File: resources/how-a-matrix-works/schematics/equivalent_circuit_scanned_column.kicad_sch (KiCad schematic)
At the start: 10 parts

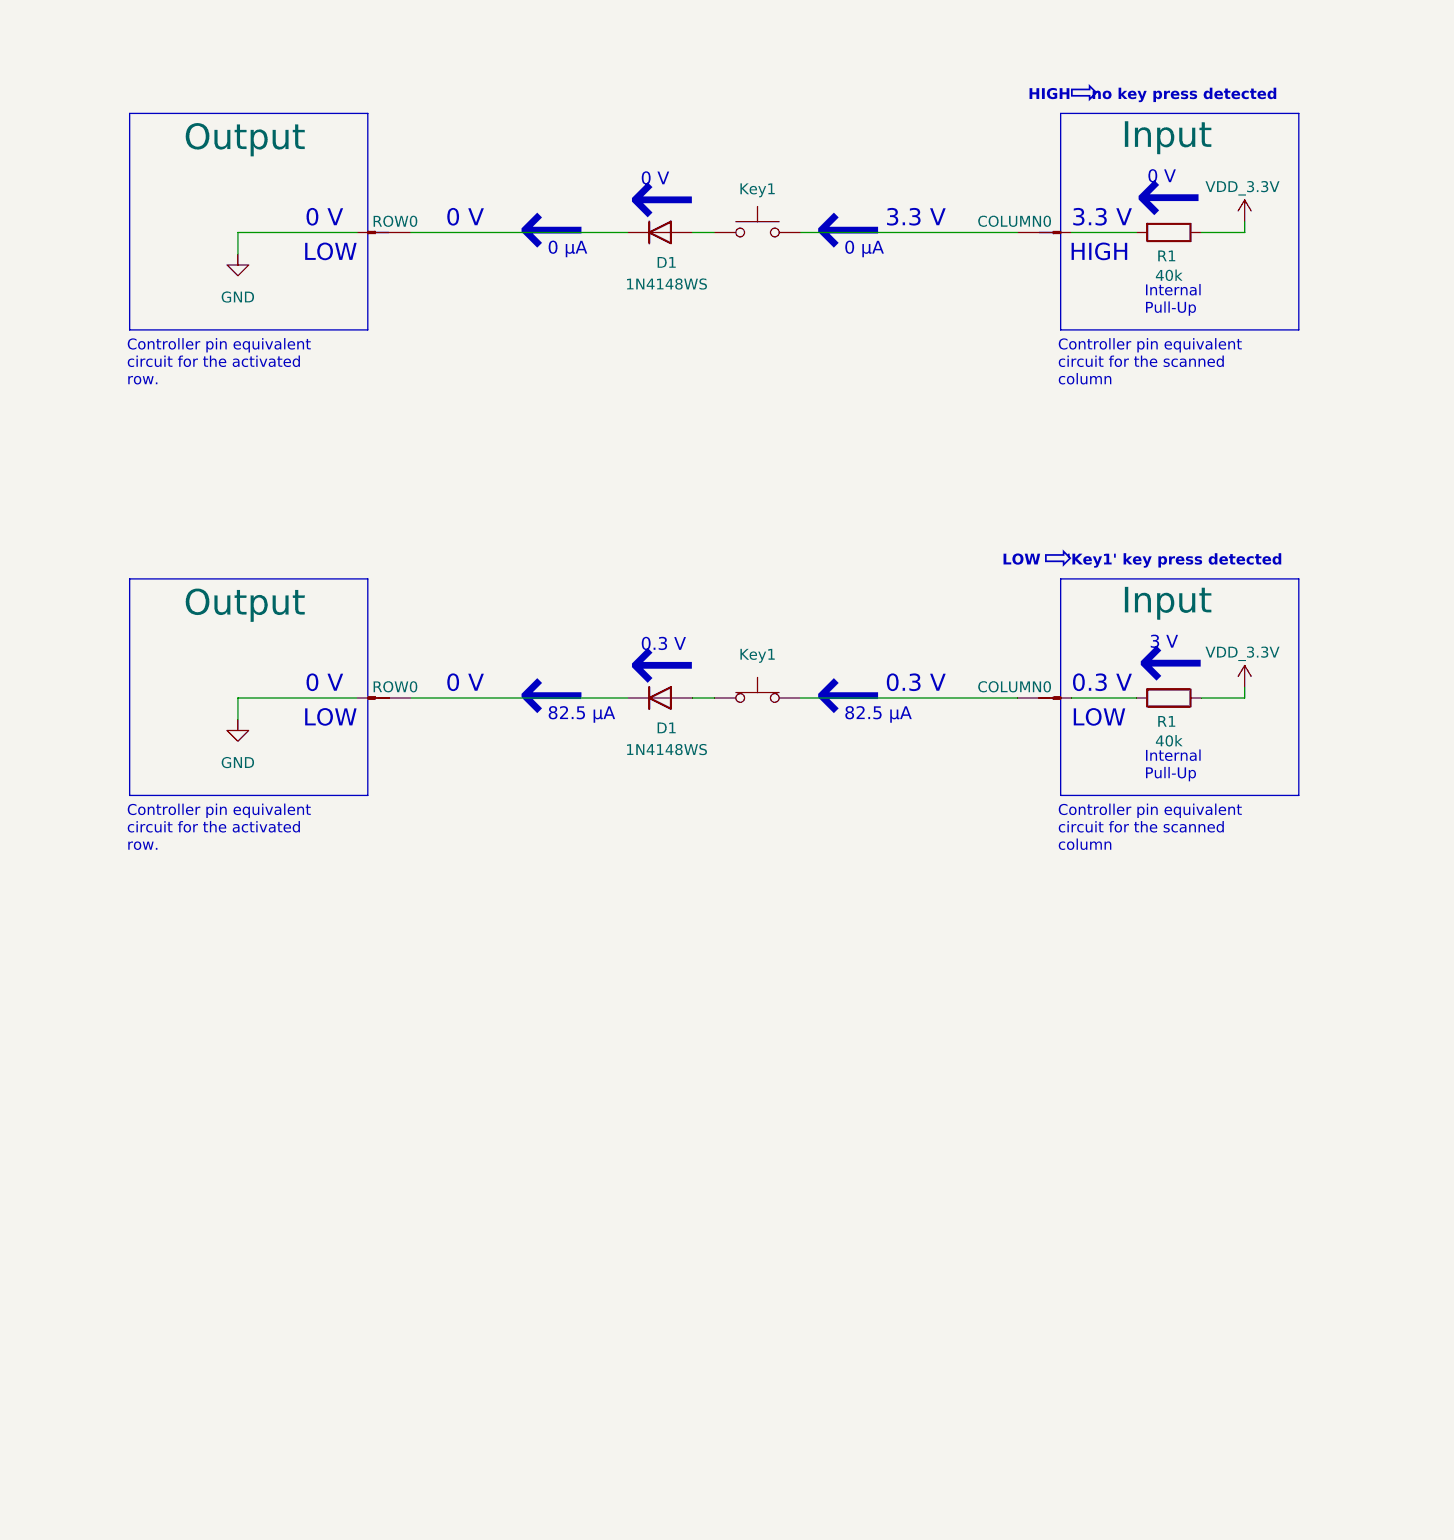
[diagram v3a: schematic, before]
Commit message: refactor equivalent circuit schematic and images
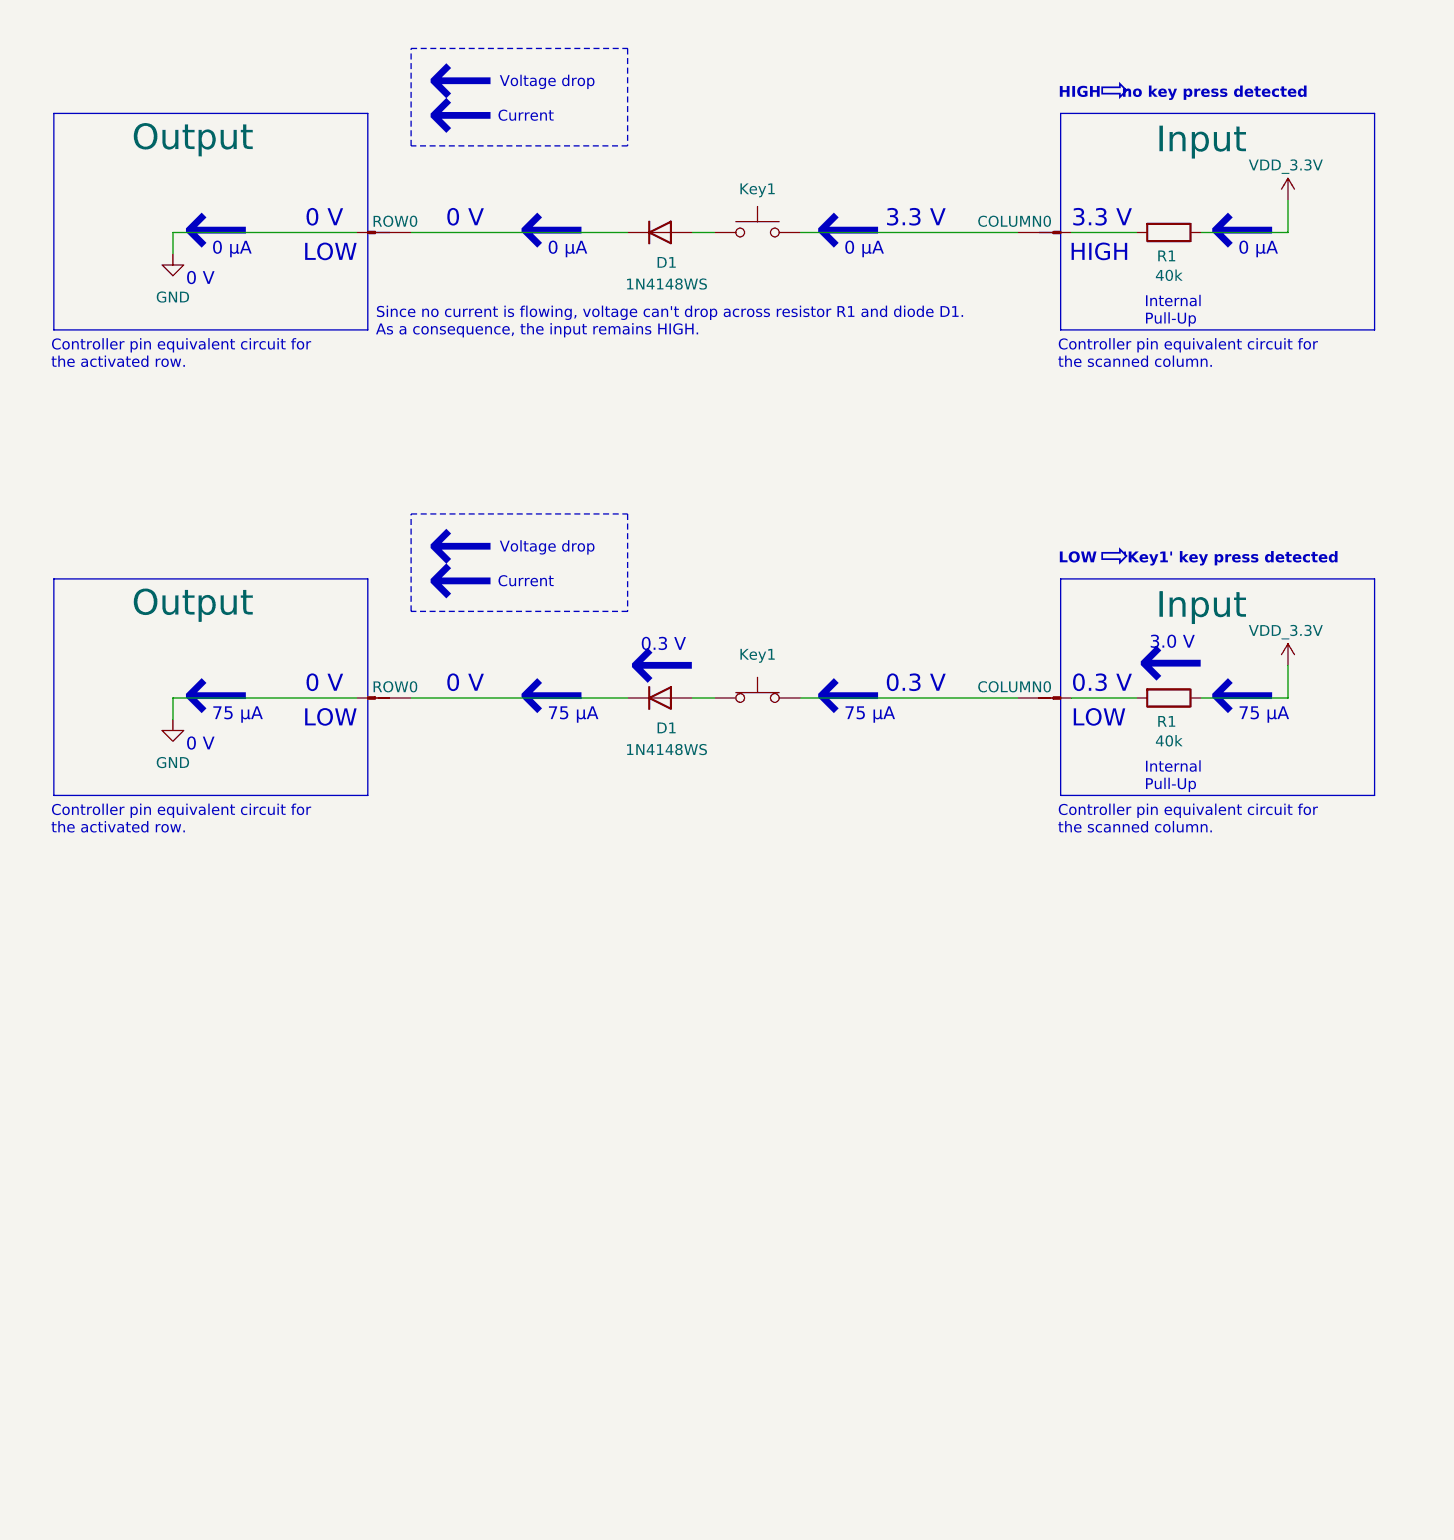
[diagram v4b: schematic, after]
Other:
- note added: "3.0 V"
- note added: "75 µA"
- note added: "Current"
- note added: "Voltage drop"
- note removed: "3 V"
- note removed: "82.5 µA"
